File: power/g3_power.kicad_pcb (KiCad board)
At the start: 4 copper layers, 50 x 40 mm, 56 parts, among them J101 533980271_Molex, J102 533980271_Molex, J103 53398-0871, SW101 SW_Push, U101 RT9471GQW, U102 TPS61202DRC, U103 LM358, U104 MCP3422

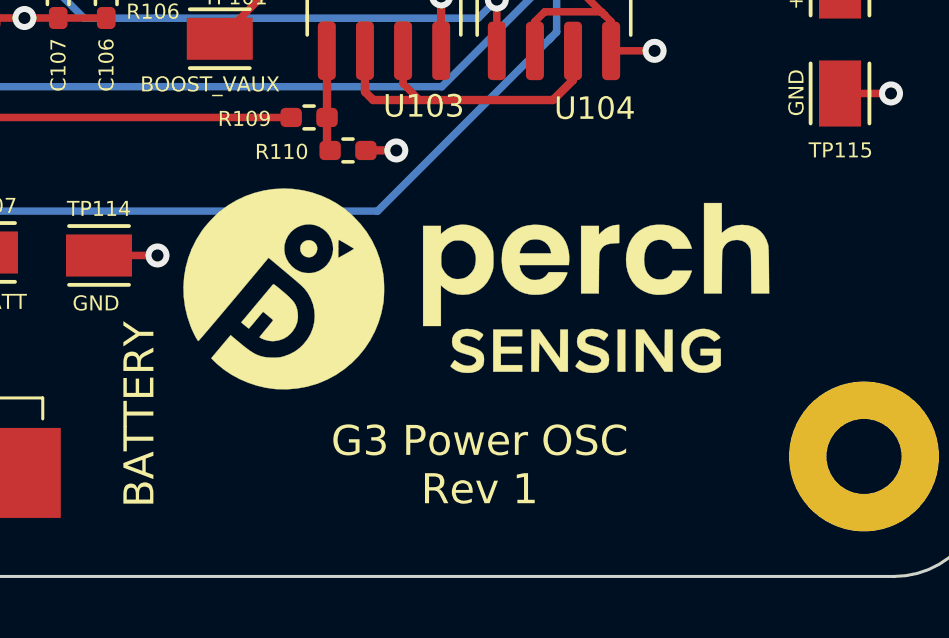
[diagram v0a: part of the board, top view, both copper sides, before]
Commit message: Adding board part number
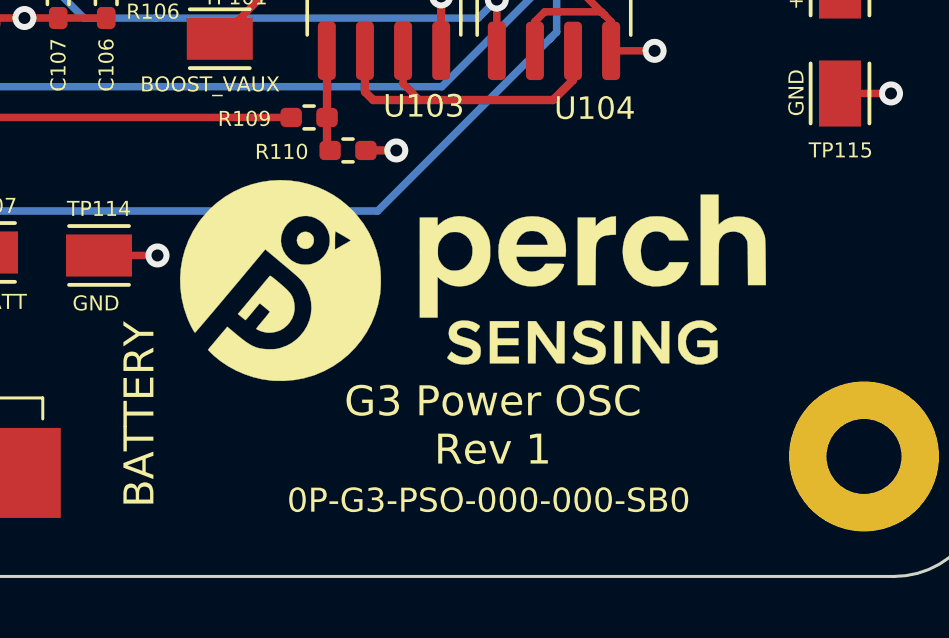
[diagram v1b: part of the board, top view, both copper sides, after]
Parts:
- moved G*** 0.30 mm to (242.1, 100.2)
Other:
- board text added: "0P-G3-PSO-000-000-SB0"
